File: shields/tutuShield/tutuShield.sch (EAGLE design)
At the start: 19 parts, among them IC1 IC_MSGEQ7-SOIC8

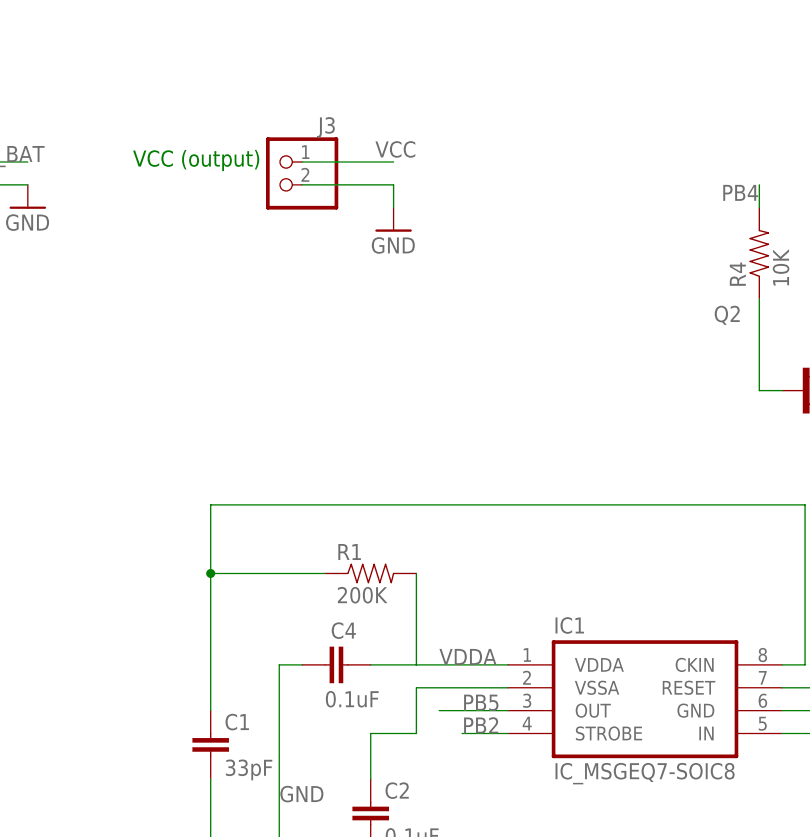
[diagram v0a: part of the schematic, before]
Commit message: fixed vcc wire bugs
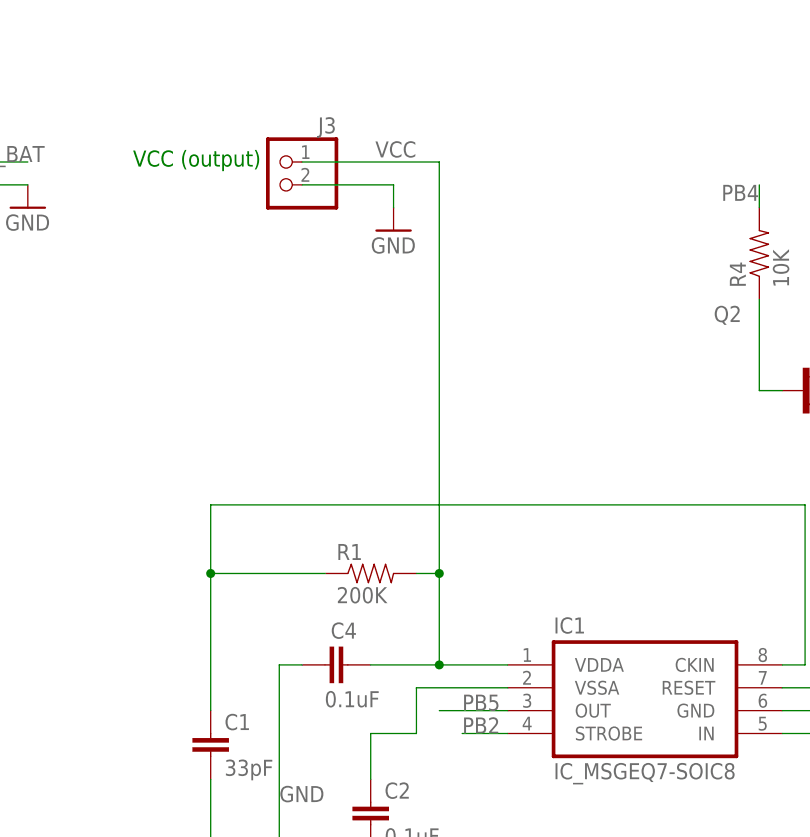
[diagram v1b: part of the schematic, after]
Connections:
- removed net VDDA: C4.2, IC1.VDDA, R1.2
- net VCC: now also C4.2, IC1.VDDA, R1.2
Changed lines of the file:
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@@
-</segment>
-</net>
-<net name="VCC" class="0">
-<segment>
-<pinref part="J3" gate="G$1" pin="1"/>
-<wire x1="88.9" y1="144.78" x2="78.74" y2="144.78" width="0.1524" layer="91"/>
-<label x="86.868" y="145.288" size="1.778" layer="95"/>
 </segment>
 </net>
@@
 </segment>
 </net>
-<net name="VDDA" class="0">
-<segment>
-<pinref part="C4" gate="G$1" pin="2"/>
-<label x="93.98" y="88.9" size="1.778" layer="95"/>
-<pinref part="R1" gate="G$1" pin="2"/>
-<wire x1="91.44" y1="88.9" x2="86.36" y2="88.9" width="0.1524" layer="91"/>
-<wire x1="91.44" y1="99.06" x2="91.44" y2="88.9" width="0.1524" layer="91"/>
-<pinref part="IC1" gate="IC" pin="VDDA"/>
-<wire x1="91.44" y1="88.9" x2="101.6" y2="88.9" width="0.1524" layer="91"/>
-</segment>
-</net>
 <net name="N$1" class="0">
 <segment>
@@
 </segment>
 </net>
+<net name="VCC" class="0">
+<segment>
+<pinref part="IC1" gate="IC" pin="VDDA"/>
+<pinref part="C4" gate="G$1" pin="2"/>
+<wire x1="101.6" y1="88.9" x2="93.98" y2="88.9" width="0.1524" layer="91"/>
+<pinref part="R1" gate="G$1" pin="2"/>
+<wire x1="93.98" y1="88.9" x2="86.36" y2="88.9" width="0.1524" layer="91"/>
+<wire x1="91.44" y1="99.06" x2="93.98" y2="99.06" width="0.1524" layer="91"/>
+<wire x1="93.98" y1="99.06" x2="93.98" y2="88.9" width="0.1524" layer="91"/>
+<junction x="93.98" y="88.9"/>
+<pinref part="J3" gate="G$1" pin="1"/>
+<wire x1="93.98" y1="144.78" x2="78.74" y2="144.78" width="0.1524" layer="91"/>
+<label x="86.868" y="145.288" size="1.778" layer="95"/>
+<wire x1="93.98" y1="144.78" x2="93.98" y2="99.06" width="0.1524" layer="91"/>
+<junction x="93.98" y="99.06"/>
+</segment>
+</net>

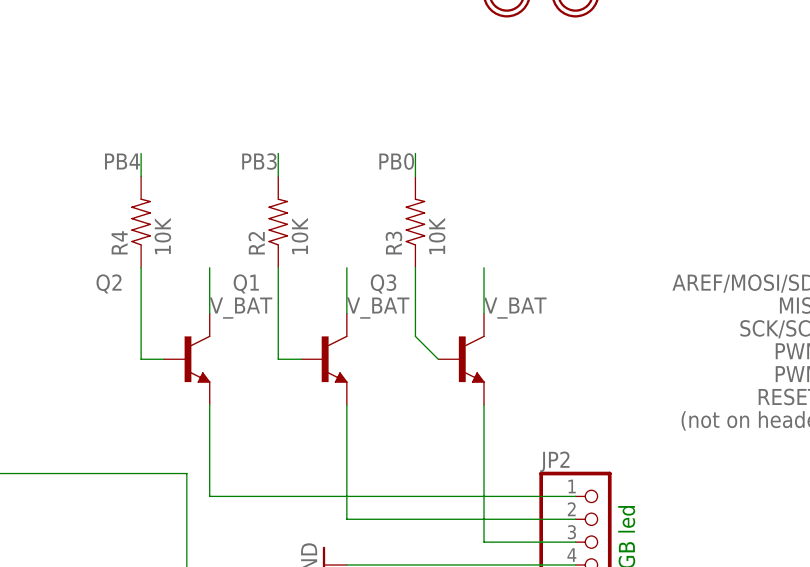
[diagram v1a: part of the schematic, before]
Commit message: fixed sizes of silkscreen fonts (was smaller then 32mil)
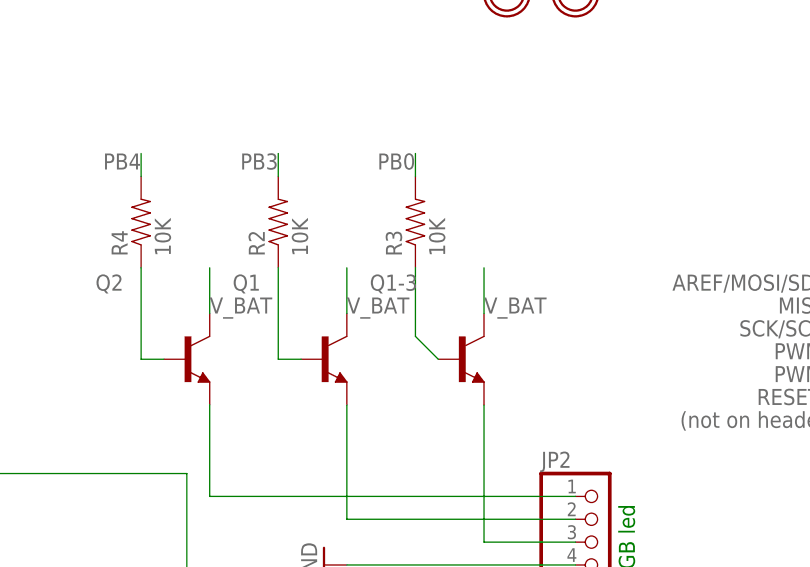
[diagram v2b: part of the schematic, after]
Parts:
- renumbered Q3 to Q1-3
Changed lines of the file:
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@@
 <?xml version="1.0" encoding="utf-8"?>
 <!DOCTYPE eagle SYSTEM "eagle.dtd">
-<eagle version="7.2.0">
+<eagle version="7.1.0">
 <drawing>
 <settings>
@@
 <part name="Q2" library="dp_devices" deviceset="TRANSISTOR_BJT_NPN" device="-SOT-23-BEC"/>
 <part name="Q1" library="dp_devices" deviceset="TRANSISTOR_BJT_NPN" device="-SOT-23-BEC"/>
-<part name="Q3" library="dp_devices" deviceset="TRANSISTOR_BJT_NPN" device="-SOT-23-BEC"/>
+<part name="Q1-3" library="dp_devices" deviceset="TRANSISTOR_BJT_NPN" device="-SOT-23-BEC"/>
 <part name="R2" library="ATtami" deviceset="RESISTOR" device="0805-RES" value="10K"/>
 <part name="R3" library="ATtami" deviceset="RESISTOR" device="0805-RES" value="10K"/>
@@
 <instance part="Q2" gate="Q" x="134.62" y="119.38"/>
 <instance part="Q1" gate="Q" x="149.86" y="119.38"/>
-<instance part="Q3" gate="Q" x="165.1" y="119.38"/>
+<instance part="Q1-3" gate="Q" x="165.1" y="119.38"/>
 <instance part="R2" gate="G$1" x="144.78" y="134.62" rot="R90"/>
 <instance part="R3" gate="G$1" x="160.02" y="134.62" rot="R90"/>
@@
 </segment>
 <segment>
-<pinref part="Q3" gate="Q" pin="C"/>
+<pinref part="Q1-3" gate="Q" pin="C"/>
 <wire x1="167.64" y1="124.46" x2="167.64" y2="129.54" width="0.1524" layer="91"/>
 <label x="167.64" y="124.46" size="1.778" layer="95"/>
@@
 <segment>
 <pinref part="R3" gate="G$1" pin="1"/>
-<pinref part="Q3" gate="Q" pin="B"/>
+<pinref part="Q1-3" gate="Q" pin="B"/>
 <wire x1="160.02" y1="129.54" x2="160.02" y2="121.92" width="0.1524" layer="91"/>
 <wire x1="160.02" y1="121.92" x2="162.56" y2="119.38" width="0.1524" layer="91"/>
@@
 <net name="N$13" class="0">
 <segment>
-<pinref part="Q3" gate="Q" pin="E"/>
+<pinref part="Q1-3" gate="Q" pin="E"/>
 <wire x1="167.64" y1="114.3" x2="167.64" y2="99.06" width="0.1524" layer="91"/>
 <pinref part="JP2" gate="A" pin="3"/>

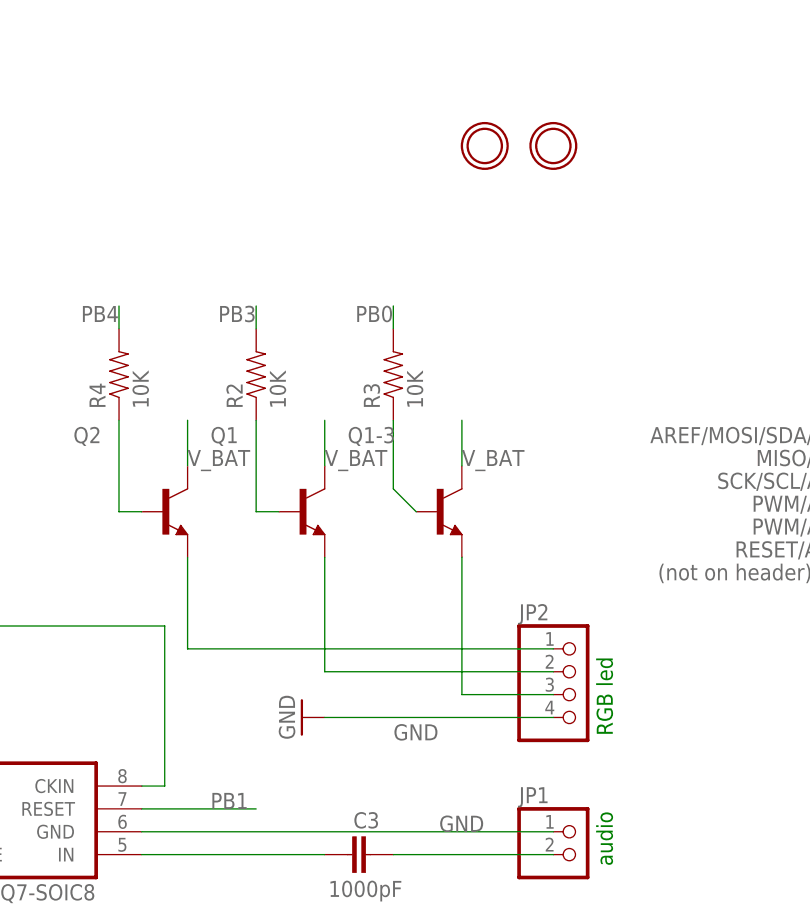
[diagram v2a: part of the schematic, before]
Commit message: rewire the npn transistors
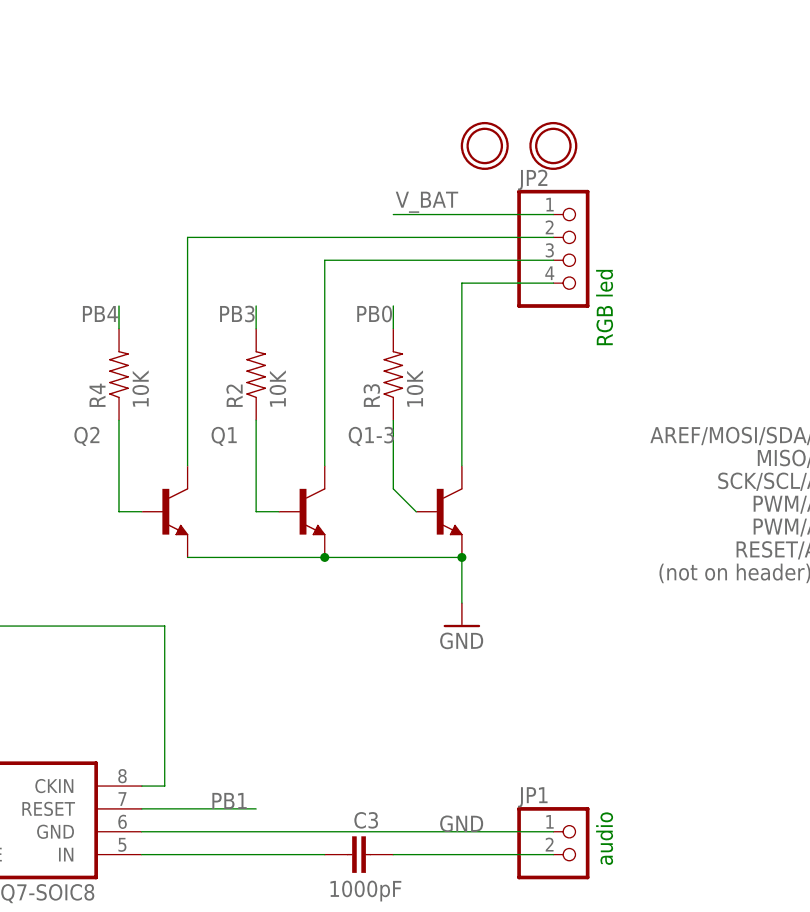
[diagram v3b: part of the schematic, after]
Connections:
- removed net N$10: JP2.1, Q2.E
- removed net N$11: JP2.2, Q1.E
- removed net N$13: JP2.3, Q1-3.E
- new net N$14: JP2.3, Q1.C
- new net N$4: JP2.2, Q2.C
- new net N$8: JP2.4, Q1-3.C
- net GND: now also Q1-3.E, Q1.E, Q2.E; no longer JP2.4
- net V_BAT: now also JP2.1; no longer Q1-3.C, Q1.C, Q2.C
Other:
- moved on the sheet: JP2
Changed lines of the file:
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@@
 </text>
 <text x="184.404" y="80.01" size="1.778" layer="91" rot="R90">audio</text>
-<text x="184.404" y="94.488" size="1.778" layer="91" rot="R90">RGB led </text>
+<text x="184.404" y="137.668" size="1.778" layer="91" rot="R90">RGB led </text>
 </plain>
 <instances>
@@
 <instance part="R3" gate="G$1" x="160.02" y="134.62" rot="R90"/>
 <instance part="R4" gate="G$1" x="129.54" y="134.62" rot="R90"/>
-<instance part="JP2" gate="A" x="180.34" y="104.14"/>
-<instance part="GND3" gate="1" x="149.86" y="96.52" rot="R270"/>
+<instance part="JP2" gate="A" x="180.34" y="152.4"/>
+<instance part="GND3" gate="1" x="167.64" y="106.68"/>
 </instances>
 <busses>
@@
 </segment>
 <segment>
-<pinref part="JP2" gate="A" pin="4"/>
-<wire x1="177.8" y1="96.52" x2="152.4" y2="96.52" width="0.1524" layer="91"/>
-<label x="160.02" y="93.98" size="1.778" layer="95"/>
-<pinref part="GND3" gate="1" pin="GND"/>
-</segment>
-<segment>
 <pinref part="JP1" gate="G$1" pin="1"/>
 <pinref part="IC1" gate="IC" pin="GND"/>
@@
 <label x="165.1" y="83.82" size="1.778" layer="95"/>
 </segment>
+<segment>
+<pinref part="Q2" gate="Q" pin="E"/>
+<pinref part="Q1" gate="Q" pin="E"/>
+<wire x1="137.16" y1="114.3" x2="152.4" y2="114.3" width="0.1524" layer="91"/>
+<pinref part="Q1-3" gate="Q" pin="E"/>
+<wire x1="152.4" y1="114.3" x2="167.64" y2="114.3" width="0.1524" layer="91"/>
+<junction x="152.4" y="114.3"/>
+<wire x1="167.64" y1="114.3" x2="167.64" y2="109.22" width="0.1524" layer="91"/>
+<junction x="167.64" y="114.3"/>
+<pinref part="GND3" gate="1" pin="GND"/>
+</segment>
 </net>
 <net name="V_BAT" class="0">
@@
 </segment>
 <segment>
-<pinref part="Q2" gate="Q" pin="C"/>
-<wire x1="137.16" y1="124.46" x2="137.16" y2="129.54" width="0.1524" layer="91"/>
-<label x="137.16" y="124.46" size="1.778" layer="95"/>
-</segment>
-<segment>
-<pinref part="Q1" gate="Q" pin="C"/>
-<wire x1="152.4" y1="124.46" x2="152.4" y2="129.54" width="0.1524" layer="91"/>
-<label x="152.4" y="124.46" size="1.778" layer="95"/>
-</segment>
-<segment>
-<pinref part="Q1-3" gate="Q" pin="C"/>
-<wire x1="167.64" y1="124.46" x2="167.64" y2="129.54" width="0.1524" layer="91"/>
-<label x="167.64" y="124.46" size="1.778" layer="95"/>
+<wire x1="177.8" y1="152.4" x2="160.02" y2="152.4" width="0.1524" layer="91"/>
+<label x="160.274" y="153.162" size="1.778" layer="95"/>
+<pinref part="JP2" gate="A" pin="1"/>
 </segment>
 </net>
@@
 <wire x1="129.54" y1="129.54" x2="129.54" y2="119.38" width="0.1524" layer="91"/>
 <wire x1="129.54" y1="119.38" x2="132.08" y2="119.38" width="0.1524" layer="91"/>
-</segment>
-</net>
-<net name="N$10" class="0">
-<segment>
-<pinref part="Q2" gate="Q" pin="E"/>
-<wire x1="137.16" y1="114.3" x2="137.16" y2="104.14" width="0.1524" layer="91"/>
-<pinref part="JP2" gate="A" pin="1"/>
-<wire x1="177.8" y1="104.14" x2="137.16" y2="104.14" width="0.1524" layer="91"/>
-</segment>
-</net>
-<net name="N$11" class="0">
-<segment>
-<pinref part="Q1" gate="Q" pin="E"/>
-<wire x1="152.4" y1="114.3" x2="152.4" y2="101.6" width="0.1524" layer="91"/>
-<pinref part="JP2" gate="A" pin="2"/>
-<wire x1="152.4" y1="101.6" x2="177.8" y2="101.6" width="0.1524" layer="91"/>
-</segment>
-</net>
-<net name="N$13" class="0">
-<segment>
-<pinref part="Q1-3" gate="Q" pin="E"/>
-<wire x1="167.64" y1="114.3" x2="167.64" y2="99.06" width="0.1524" layer="91"/>
-<pinref part="JP2" gate="A" pin="3"/>
-<wire x1="167.64" y1="99.06" x2="177.8" y2="99.06" width="0.1524" layer="91"/>
 </segment>
 </net>
@@
 </segment>
 </net>
+<net name="N$8" class="0">
+<segment>
+<pinref part="Q1-3" gate="Q" pin="C"/>
+<wire x1="167.64" y1="124.46" x2="167.64" y2="144.78" width="0.1524" layer="91"/>
+<pinref part="JP2" gate="A" pin="4"/>
+<wire x1="167.64" y1="144.78" x2="177.8" y2="144.78" width="0.1524" layer="91"/>
+</segment>
+</net>
+<net name="N$14" class="0">
+<segment>
+<pinref part="Q1" gate="Q" pin="C"/>
+<wire x1="152.4" y1="124.46" x2="152.4" y2="147.32" width="0.1524" layer="91"/>
+<pinref part="JP2" gate="A" pin="3"/>
+<wire x1="152.4" y1="147.32" x2="177.8" y2="147.32" width="0.1524" layer="91"/>
+</segment>
+</net>
+<net name="N$4" class="0">
+<segment>
+<pinref part="Q2" gate="Q" pin="C"/>
+<wire x1="137.16" y1="149.86" x2="137.16" y2="124.46" width="0.1524" layer="91"/>
+<pinref part="JP2" gate="A" pin="2"/>
+<wire x1="177.8" y1="149.86" x2="137.16" y2="149.86" width="0.1524" layer="91"/>
+</segment>
+</net>

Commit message: fixed pwm misshap in tutu shield
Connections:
- net PB1: now also R2.2; no longer IC1.RESET
- net PB3: now also IC1.RESET; no longer R2.2
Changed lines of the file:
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@@
 </segment>
 <segment>
-<pinref part="IC1" gate="IC" pin="RESET"/>
-<wire x1="132.08" y1="86.36" x2="144.78" y2="86.36" width="0.1524" layer="91"/>
-<label x="139.7" y="86.36" size="1.778" layer="95"/>
+<pinref part="R2" gate="G$1" pin="2"/>
+<wire x1="144.78" y1="139.7" x2="144.78" y2="142.24" width="0.1524" layer="91"/>
+<label x="144.78" y="142.24" size="1.778" layer="95" rot="R180"/>
 </segment>
 </net>
@@
 </segment>
 <segment>
-<pinref part="R2" gate="G$1" pin="2"/>
-<wire x1="144.78" y1="139.7" x2="144.78" y2="142.24" width="0.1524" layer="91"/>
-<label x="144.78" y="142.24" size="1.778" layer="95" rot="R180"/>
+<pinref part="IC1" gate="IC" pin="RESET"/>
+<wire x1="132.08" y1="86.36" x2="147.32" y2="86.36" width="0.1524" layer="91"/>
+<label x="142.24" y="86.36" size="1.778" layer="95"/>
 </segment>
 </net>
